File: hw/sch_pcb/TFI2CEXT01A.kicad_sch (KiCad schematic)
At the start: 17 parts, among them J2 SM04B-GHS-TB, J3 SM04B-GHS-TB, M2 M3, U3 MIC5504-3.3YM5

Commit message: Add secondary input connector #2.
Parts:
- added J?: SM04B-GHS-TB, Connector_JST:JST_GH_SM04B-GHS-TB_1x04-1MP_P1.25mm_Horizontal, symbol MLAB_CONNECTORS_JST:SM04B-GHS-TB
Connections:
- net +5V: now also J?.1
- net GND: now also J?.4, J?.MP
- net SCLin: now also J?.2
- net SDAin: now also J?.3
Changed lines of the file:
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@@
   (junction (at 81.28 168.91) (diameter 1.016) (color 0 0 0 0))
   (junction (at 91.44 102.87) (diameter 1.016) (color 0 0 0 0))
+  (junction (at 91.44 133.985) (diameter 1.016) (color 0 0 0 0))
   (junction (at 97.79 95.25) (diameter 1.016) (color 0 0 0 0))
   (junction (at 104.14 97.79) (diameter 1.016) (color 0 0 0 0))
@@
     (stroke (width 0) (type solid) (color 0 0 0 0))
   )
+  (wire (pts (xy 90.17 126.365) (xy 97.79 126.365))
+    (stroke (width 0) (type solid) (color 0 0 0 0))
+  )
+  (wire (pts (xy 90.17 128.905) (xy 97.79 128.905))
+    (stroke (width 0) (type solid) (color 0 0 0 0))
+  )
+  (wire (pts (xy 90.17 131.445) (xy 91.44 131.445))
+    (stroke (width 0) (type solid) (color 0 0 0 0))
+  )
+  (wire (pts (xy 90.17 133.985) (xy 91.44 133.985))
+    (stroke (width 0) (type solid) (color 0 0 0 0))
+  )
   (wire (pts (xy 91.44 82.55) (xy 91.44 92.71))
     (stroke (width 0) (type solid) (color 0 0 0 0))
@@
   )
   (wire (pts (xy 91.44 102.87) (xy 91.44 106.68))
+    (stroke (width 0) (type solid) (color 0 0 0 0))
+  )
+  (wire (pts (xy 91.44 119.38) (xy 91.44 123.825))
+    (stroke (width 0) (type solid) (color 0 0 0 0))
+  )
+  (wire (pts (xy 91.44 123.825) (xy 90.17 123.825))
+    (stroke (width 0) (type solid) (color 0 0 0 0))
+  )
+  (wire (pts (xy 91.44 131.445) (xy 91.44 133.985))
+    (stroke (width 0) (type solid) (color 0 0 0 0))
+  )
+  (wire (pts (xy 91.44 133.985) (xy 91.44 137.795))
     (stroke (width 0) (type solid) (color 0 0 0 0))
   )
@@
     (effects (font (size 1.524 1.524)) (justify right bottom))
   )
+  (label "SCLin" (at 97.79 126.365 180)
+    (effects (font (size 1.524 1.524)) (justify right bottom))
+  )
+  (label "SDAin" (at 97.79 128.905 180)
+    (effects (font (size 1.524 1.524)) (justify right bottom))
+  )
   (label "EN" (at 115.57 101.6 180)
     (effects (font (size 1.524 1.524)) (justify right bottom))
@@
     (pin "1")
   )
+  (symbol (lib_id "power:+5V") (at 91.44 119.38 0) (mirror y) (unit 1)
+    (in_bom yes) (on_board yes)
+    (property "Reference" "#PWR?" (id 0) (at 91.44 123.19 0)
+      (effects (font (size 1.27 1.27)) hide)
+    )
+    (property "Value" "+5V" (id 1) (at 91.059 114.9858 0))
+    (property "Footprint" "" (id 2) (at 91.44 119.38 0)
+      (effects (font (size 1.27 1.27)) hide)
+    )
+    (property "Datasheet" "" (id 3) (at 91.44 119.38 0)
+      (effects (font (size 1.27 1.27)) hide)
+    )
+    (pin "1")
+  )
   (symbol (lib_id "power:+3V3") (at 97.79 82.55 0) (unit 1)
     (in_bom yes) (on_board yes)
@@
     )
     (property "Datasheet" "" (id 3) (at 91.44 106.68 0)
+      (effects (font (size 1.27 1.27)) hide)
+    )
+    (pin "1")
+  )
+  (symbol (lib_id "power:GND") (at 91.44 137.795 0) (mirror y) (unit 1)
+    (in_bom yes) (on_board yes)
+    (property "Reference" "#PWR?" (id 0) (at 91.44 144.145 0)
+      (effects (font (size 1.27 1.27)) hide)
+    )
+    (property "Value" "GND" (id 1) (at 91.313 142.1892 0))
+    (property "Footprint" "" (id 2) (at 91.44 137.795 0)
+      (effects (font (size 1.27 1.27)) hide)
+    )
+    (property "Datasheet" "" (id 3) (at 91.44 137.795 0)
       (effects (font (size 1.27 1.27)) hide)
     )
@@
     )
     (property "UST_ID" "5c86273d1287500b4e0280be" (id 5) (at 85.09 97.79 0)
+      (effects (font (size 1.27 1.27)) hide)
+    )
+    (pin "1")
+    (pin "2")
+    (pin "3")
+    (pin "4")
+    (pin "MP")
+  )
+  (symbol (lib_id "MLAB_CONNECTORS_JST:SM04B-GHS-TB") (at 85.09 128.905 0) (mirror y) (unit 1)
+    (in_bom yes) (on_board yes)
+    (property "Reference" "J?" (id 0) (at 83.1088 127.4064 0)
+      (effects (font (size 1.524 1.524)) (justify left))
+    )
+    (property "Value" "SM04B-GHS-TB" (id 1) (at 83.1088 130.1242 0)
+      (effects (font (size 1.524 1.524)) (justify left))
+    )
+    (property "Footprint" "Connector_JST:JST_GH_SM04B-GHS-TB_1x04-1MP_P1.25mm_Horizontal" (id 2) (at 85.09 123.825 0)
+      (effects (font (size 1.524 1.524)) hide)
+    )
+    (property "Datasheet" "" (id 3) (at 85.09 123.825 0)
+      (effects (font (size 1.524 1.524)))
+    )
+    (property "UST_id" "" (id 4) (at 85.09 128.905 0)
+      (effects (font (size 1.27 1.27)) hide)
+    )
+    (property "UST_ID" "5c86273d1287500b4e0280be" (id 5) (at 85.09 128.905 0)
       (effects (font (size 1.27 1.27)) hide)
     )
@@
       (reference "#PWR?") (unit 1) (value "GND") (footprint "")
     )
+    (path "/1df0862e-b632-4bdd-aa64-2038cb83123b"
+      (reference "#PWR?") (unit 1) (value "GND") (footprint "")
+    )
     (path "/584dadcd-f462-4861-8cc5-b38ddf8e690a"
       (reference "#PWR?") (unit 1) (value "GND") (footprint "")
     )
+    (path "/6ed52263-58db-4a97-82f4-86b9f09e3aa9"
+      (reference "#PWR?") (unit 1) (value "+5V") (footprint "")
+    )
     (path "/712f2299-6d07-4921-b3fc-2767cf7d943a"
       (reference "#PWR?") (unit 1) (value "+3V3") (footprint "")
@@
       (reference "J3") (unit 1) (value "SM04B-GHS-TB") (footprint "Connector_JST:JST_GH_SM04B-GHS-TB_1x04-1MP_P1.25mm_Horizontal")
     )
+    (path "/acfde87a-c369-4ef9-b4fe-c0d5b5b283eb"
+      (reference "J?") (unit 1) (value "SM04B-GHS-TB") (footprint "Connector_JST:JST_GH_SM04B-GHS-TB_1x04-1MP_P1.25mm_Horizontal")
+    )
     (path "/cb19bc52-bc73-4faa-b1b5-9d6fa377e0e1"

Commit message: The first layout
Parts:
- added D1: LED GREEN, Mlab_D:LED_1206, symbol Device:LED
- added R1: 180R, Mlab_R:SMD-0603, symbol Device:R
- D2: renamed from D1; value ZENER-6.2V -> BZX585-B5V6.115; footprint Mlab_D:Diode-MiniMELF_Standard -> Diode_SMD:D_SOD-523
- R4: value 51R -> 180R; UST_ID 5c70984512875079b91f8953 -> (none)
- gave numbers to parts that had none: 5
- renumbered C3 to C1, C4 to C2, C1 to C3, C5 to C4, D2 to D3, J3 to J1, J2 to J3, M2 to M1, R10 to R5, R3 to R6, U3 to U1
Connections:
- net +5V: now also R1.1
- net GND: now also D1.1 (K)
- new net: D1.2 (A), R1.2
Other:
- note removed: "BZX585-B5V6.115 NEXPERIA"

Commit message: Edit PCB
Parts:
- added M2, M3, M4, M5, M6: HOLE, Mlab_Mechanical:dira_3mm, symbol MLAB_MECHANICAL:HOLE
- M1: value M3 -> HOLE; footprint Mlab_Mechanical:MountingHole_3mm -> Mlab_Mechanical:dira_3mm
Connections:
- net GND: no longer M1.1
- no-connect marks 0 -> 6
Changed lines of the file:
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@@
-(kicad_sch (version 20210126) (generator eeschema)
+(kicad_sch (version 20210406) (generator eeschema)
   (paper "A4")
   (title_block
@@
   (junction (at 161.29 102.87) (diameter 1.016) (color 0 0 0 0))
   (junction (at 161.29 129.54) (diameter 1.016) (color 0 0 0 0))
+  (no_connect (at 228.6 20.32))
+  (no_connect (at 237.49 20.32))
+  (no_connect (at 246.38 20.32))
+  (no_connect (at 255.27 20.32))
+  (no_connect (at 264.16 20.32))
+  (no_connect (at 273.05 20.32))
   (wire (pts (xy 19.05 163.83) (xy 19.05 165.1))
     (stroke (width 0) (type solid) (color 0 0 0 0))
@@
     (stroke (width 0) (type solid) (color 0 0 0 0))
   )
-  (wire (pts (xy 265.43 20.32) (xy 265.43 19.05))
-    (stroke (width 0) (type solid) (color 0 0 0 0))
-  )
-  (wire (pts (xy 270.51 19.05) (xy 265.43 19.05))
-    (stroke (width 0) (type solid) (color 0 0 0 0))
-  )
-  (wire (pts (xy 270.51 20.32) (xy 270.51 19.05))
-    (stroke (width 0) (type solid) (color 0 0 0 0))
-  )
-  (polyline (pts (xy 255.27 17.78) (xy 280.67 17.78))
+  (polyline (pts (xy 226.06 17.78) (xy 229.87 17.78))
     (stroke (width 0) (type dash) (color 0 0 0 0))
   )
-  (polyline (pts (xy 255.27 27.94) (xy 255.27 17.78))
+  (polyline (pts (xy 226.06 27.94) (xy 226.06 17.78))
+    (stroke (width 0) (type dash) (color 0 0 0 0))
+  )
+  (polyline (pts (xy 226.06 27.94) (xy 229.87 27.94))
+    (stroke (width 0) (type dash) (color 0 0 0 0))
+  )
+  (polyline (pts (xy 229.87 17.78) (xy 237.49 17.78))
+    (stroke (width 0) (type dash) (color 0 0 0 0))
+  )
+  (polyline (pts (xy 229.87 27.94) (xy 237.49 27.94))
+    (stroke (width 0) (type dash) (color 0 0 0 0))
+  )
+  (polyline (pts (xy 237.49 17.78) (xy 262.89 17.78))
+    (stroke (width 0) (type dash) (color 0 0 0 0))
+  )
+  (polyline (pts (xy 262.89 17.78) (xy 280.67 17.78))
+    (stroke (width 0) (type dash) (color 0 0 0 0))
+  )
+  (polyline (pts (xy 262.89 27.94) (xy 237.49 27.94))
+    (stroke (width 0) (type dash) (color 0 0 0 0))
+  )
+  (polyline (pts (xy 262.89 27.94) (xy 280.67 27.94))
     (stroke (width 0) (type dash) (color 0 0 0 0))
   )
@@
     (stroke (width 0) (type dash) (color 0 0 0 0))
   )
-  (polyline (pts (xy 280.67 27.94) (xy 255.27 27.94))
-    (stroke (width 0) (type dash) (color 0 0 0 0))
-  )
-  (text "MOUNTING HOLES" (at 257.81 27.94 0)
+  (text "MOUNTING HOLES" (at 240.03 27.94 0)
     (effects (font (size 1.524 1.524)) (justify left bottom))
   )
@@
     (effects (font (size 1.524 1.524)) (justify left bottom))
   )
-  (symbol (lib_id "MLAB_MECHANICAL:HOLE") (at 265.43 21.59 90) (unit 1)
-    (in_bom yes) (on_board yes)
-    (property "Reference" "M1" (id 0) (at 265.43 24.13 90)
-      (effects (font (size 1.524 1.524)))
-    )
-    (property "Value" "M3" (id 1) (at 262.89 20.32 0)
-      (effects (font (size 1.524 1.524)))
-    )
-    (property "Footprint" "Mlab_Mechanical:MountingHole_3mm" (id 2) (at 265.43 21.59 0)
-      (effects (font (size 1.524 1.524)) hide)
-    )
-    (property "Datasheet" "" (id 3) (at 265.43 21.59 0)
+  (symbol (lib_id "MLAB_MECHANICAL:HOLE") (at 228.6 21.59 90) (unit 1)
+    (in_bom yes) (on_board yes) (fields_autoplaced)
+    (property "Reference" "M1" (id 0) (at 229.9971 20.2579 90)
+      (effects (font (size 1.524 1.524)) (justify right))
+    )
+    (property "Value" "HOLE" (id 1) (at 229.9971 22.9655 90)
+      (effects (font (size 1.524 1.524)) (justify right))
+    )
+    (property "Footprint" "Mlab_Mechanical:dira_3mm" (id 2) (at 228.6 21.59 0)
+      (effects (font (size 1.524 1.524)) hide)
+    )
+    (property "Datasheet" "" (id 3) (at 228.6 21.59 0)
+      (effects (font (size 1.524 1.524)))
+    )
+    (pin "1")
+  )
+  (symbol (lib_id "MLAB_MECHANICAL:HOLE") (at 237.49 21.59 90) (unit 1)
+    (in_bom yes) (on_board yes) (fields_autoplaced)
+    (property "Reference" "M2" (id 0) (at 238.8871 20.2579 90)
+      (effects (font (size 1.524 1.524)) (justify right))
+    )
+    (property "Value" "HOLE" (id 1) (at 238.8871 22.9655 90)
+      (effects (font (size 1.524 1.524)) (justify right))
+    )
+    (property "Footprint" "Mlab_Mechanical:dira_3mm" (id 2) (at 237.49 21.59 0)
+      (effects (font (size 1.524 1.524)) hide)
+    )
+    (property "Datasheet" "" (id 3) (at 237.49 21.59 0)
+      (effects (font (size 1.524 1.524)))
+    )
+    (pin "1")
+  )
+  (symbol (lib_id "MLAB_MECHANICAL:HOLE") (at 246.38 21.59 90) (unit 1)
+    (in_bom yes) (on_board yes)
+    (property "Reference" "M3" (id 0) (at 247.7771 20.2579 90)
+      (effects (font (size 1.524 1.524)) (justify right))
+    )
+    (property "Value" "HOLE" (id 1) (at 247.7771 22.9655 90)
+      (effects (font (size 1.524 1.524)) (justify right))
+    )
+    (property "Footprint" "Mlab_Mechanical:dira_3mm" (id 2) (at 246.38 21.59 0)
+      (effects (font (size 1.524 1.524)) hide)
+    )
+    (property "Datasheet" "" (id 3) (at 246.38 21.59 0)
+      (effects (font (size 1.524 1.524)))
+    )
+    (pin "1")
+  )
+  (symbol (lib_id "MLAB_MECHANICAL:HOLE") (at 255.27 21.59 90) (unit 1)
+    (in_bom yes) (on_board yes) (fields_autoplaced)
+    (property "Reference" "M4" (id 0) (at 256.6671 20.2579 90)
+      (effects (font (size 1.524 1.524)) (justify right))
+    )
+    (property "Value" "HOLE" (id 1) (at 256.6671 22.9655 90)
+      (effects (font (size 1.524 1.524)) (justify right))
+    )
+    (property "Footprint" "Mlab_Mechanical:dira_3mm" (id 2) (at 255.27 21.59 0)
+      (effects (font (size 1.524 1.524)) hide)
+    )
+    (property "Datasheet" "" (id 3) (at 255.27 21.59 0)
+      (effects (font (size 1.524 1.524)))
+    )
+    (pin "1")
+  )
+  (symbol (lib_id "MLAB_MECHANICAL:HOLE") (at 264.16 21.59 90) (unit 1)
+    (in_bom yes) (on_board yes) (fields_autoplaced)
+    (property "Reference" "M5" (id 0) (at 265.5571 20.2579 90)
+      (effects (font (size 1.524 1.524)) (justify right))
+    )
+    (property "Value" "HOLE" (id 1) (at 265.5571 22.9655 90)
+      (effects (font (size 1.524 1.524)) (justify right))
+    )
+    (property "Footprint" "Mlab_Mechanical:dira_3mm" (id 2) (at 264.16 21.59 0)
+      (effects (font (size 1.524 1.524)) hide)
+    )
+    (property "Datasheet" "" (id 3) (at 264.16 21.59 0)
+      (effects (font (size 1.524 1.524)))
+    )
+    (pin "1")
+  )
+  (symbol (lib_id "MLAB_MECHANICAL:HOLE") (at 273.05 21.59 90) (unit 1)
+    (in_bom yes) (on_board yes) (fields_autoplaced)
+    (property "Reference" "M6" (id 0) (at 274.4471 20.2579 90)
+      (effects (font (size 1.524 1.524)) (justify right))
+    )
+    (property "Value" "HOLE" (id 1) (at 274.4471 22.9655 90)
+      (effects (font (size 1.524 1.524)) (justify right))
+    )
+    (property "Footprint" "Mlab_Mechanical:dira_3mm" (id 2) (at 273.05 21.59 0)
+      (effects (font (size 1.524 1.524)) hide)
+    )
+    (property "Datasheet" "" (id 3) (at 273.05 21.59 0)
       (effects (font (size 1.524 1.524)))
     )
@@
     (property "Datasheet" "" (id 3) (at 161.29 132.08 0)
       (effects (font (size 1.27 1.27)) hide)
-    )
-    (pin "1")
-  )
-  (symbol (lib_id "power:GND") (at 270.51 20.32 0) (unit 1)
-    (in_bom yes) (on_board yes)
-    (property "Reference" "#PWR027" (id 0) (at 270.51 26.67 0)
-      (effects (font (size 1.524 1.524)) hide)
-    )
-    (property "Value" "GND" (id 1) (at 270.51 24.13 0)
-      (effects (font (size 1.524 1.524)))
-    )
-    (property "Footprint" "" (id 2) (at 270.51 20.32 0)
-      (effects (font (size 1.524 1.524)))
-    )
-    (property "Datasheet" "" (id 3) (at 270.51 20.32 0)
-      (effects (font (size 1.524 1.524)))
     )
     (pin "1")
@@
       (reference "#PWR026") (unit 1) (value "GND") (footprint "")
     )
-    (path "/00000000-0000-0000-0000-0000549d770f"
-      (reference "#PWR027") (unit 1) (value "GND") (footprint "")
-    )
     (path "/00000000-0000-0000-0000-000059ffc6a8"
       (reference "C1") (unit 1) (value "10uF") (footprint "Mlab_R:SMD-0805")
@@
       (reference "J4") (unit 1) (value "SM04B-GHS-TB") (footprint "Connector_JST:JST_GH_SM04B-GHS-TB_1x04-1MP_P1.25mm_Horizontal")
     )
-    (path "/00000000-0000-0000-0000-0000549d7628"
-      (reference "M1") (unit 1) (value "M3") (footprint "Mlab_Mechanical:MountingHole_3mm")
+    (path "/99d533fb-9d70-48e2-8fd6-c2f3a8e6e539"
+      (reference "M1") (unit 1) (value "HOLE") (footprint "Mlab_Mechanical:dira_3mm")
+    )
+    (path "/5772f8cf-ad63-4406-98f0-cba007b77f95"
+      (reference "M2") (unit 1) (value "HOLE") (footprint "Mlab_Mechanical:dira_3mm")
+    )
+    (path "/274711c1-bbe2-42ee-96d7-8e3e40bc8d5d"
+      (reference "M3") (unit 1) (value "HOLE") (footprint "Mlab_Mechanical:dira_3mm")
+    )
+    (path "/21d93760-b684-44de-bfcd-0dfe3feb2abe"
+      (reference "M4") (unit 1) (value "HOLE") (footprint "Mlab_Mechanical:dira_3mm")
+    )
+    (path "/dcef6574-268c-4858-9322-b68348606397"
+      (reference "M5") (unit 1) (value "HOLE") (footprint "Mlab_Mechanical:dira_3mm")
+    )
+    (path "/19b0d29d-d7c2-446e-a8fb-72bf37c91050"
+      (reference "M6") (unit 1) (value "HOLE") (footprint "Mlab_Mechanical:dira_3mm")
     )
     (path "/d6f125ac-9f23-4a8a-8f1d-fc20a4cd2a4a"

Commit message: Edit
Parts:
- D1: UST_ID (none) -> 5c70984412875079b91f8895
- D2: UST_ID 604b0326128750769e5b0f93 -> 60879d38128750769ee58e48
- R1, R4: UST_ID (none) -> 5c70984512875079b91f8957
- R2, R3, R5, R6: UST_ID 5c70984612875079b91f899f -> 5c70984512875079b91f8962
- U2: UST_ID (none) -> 6087a3f3128750769ee58f03
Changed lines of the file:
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@@
       (effects (font (size 1.27 1.27)) hide)
     )
-    (property "UST_ID" "" (id 5) (at 19.05 168.91 0)
+    (property "UST_ID" "5c70984512875079b91f8957" (id 5) (at 19.05 168.91 0)
       (effects (font (size 1.27 1.27)) hide)
     )
@@
       (effects (font (size 1.27 1.27)) hide)
     )
-    (property "UST_ID" "5c70984612875079b91f899f" (id 5) (at 97.79 87.63 0)
+    (property "UST_ID" "5c70984512875079b91f8962" (id 5) (at 97.79 87.63 0)
       (effects (font (size 1.27 1.27)) hide)
     )
@@
       (effects (font (size 1.27 1.27)) hide)
     )
-    (property "UST_ID" "5c70984612875079b91f899f" (id 5) (at 104.14 87.63 0)
+    (property "UST_ID" "5c70984512875079b91f8962" (id 5) (at 104.14 87.63 0)
       (effects (font (size 1.27 1.27)) hide)
     )
@@
       (effects (font (size 1.27 1.27)) hide)
     )
-    (property "UST_ID" "" (id 5) (at 140.97 87.63 0)
+    (property "UST_ID" "5c70984512875079b91f8957" (id 5) (at 140.97 87.63 0)
       (effects (font (size 1.27 1.27)) hide)
     )
@@
       (effects (font (size 1.27 1.27)) hide)
     )
-    (property "UST_ID" "5c70984612875079b91f899f" (id 5) (at 147.32 87.63 0)
+    (property "UST_ID" "5c70984512875079b91f8962" (id 5) (at 147.32 87.63 0)
       (effects (font (size 1.27 1.27)) hide)
     )
@@
       (effects (font (size 1.27 1.27)) hide)
     )
-    (property "UST_ID" "5c70984612875079b91f899f" (id 5) (at 153.67 87.63 0)
+    (property "UST_ID" "5c70984512875079b91f8962" (id 5) (at 153.67 87.63 0)
       (effects (font (size 1.27 1.27)) hide)
     )
@@
       (effects (font (size 1.27 1.27)) hide)
     )
-    (property "UST_ID" "604b0326128750769e5b0f93" (id 5) (at 43.18 175.26 0)
+    (property "UST_ID" "60879d38128750769ee58e48" (id 5) (at 43.18 175.26 0)
       (effects (font (size 1.27 1.27)) hide)
     )
@@
       (effects (font (size 1.27 1.27)) hide)
     )
-    (property "UST_ID" "" (id 5) (at 19.05 177.8 0)
+    (property "UST_ID" "5c70984412875079b91f8895" (id 5) (at 19.05 177.8 0)
       (effects (font (size 1.27 1.27)) hide)
     )
@@
       (effects (font (size 1.27 1.27)) hide)
     )
+    (property "UST_ID" "6087a3f3128750769ee58f03" (id 4) (at 125.73 97.79 0)
+      (effects (font (size 1.27 1.27)) hide)
+    )

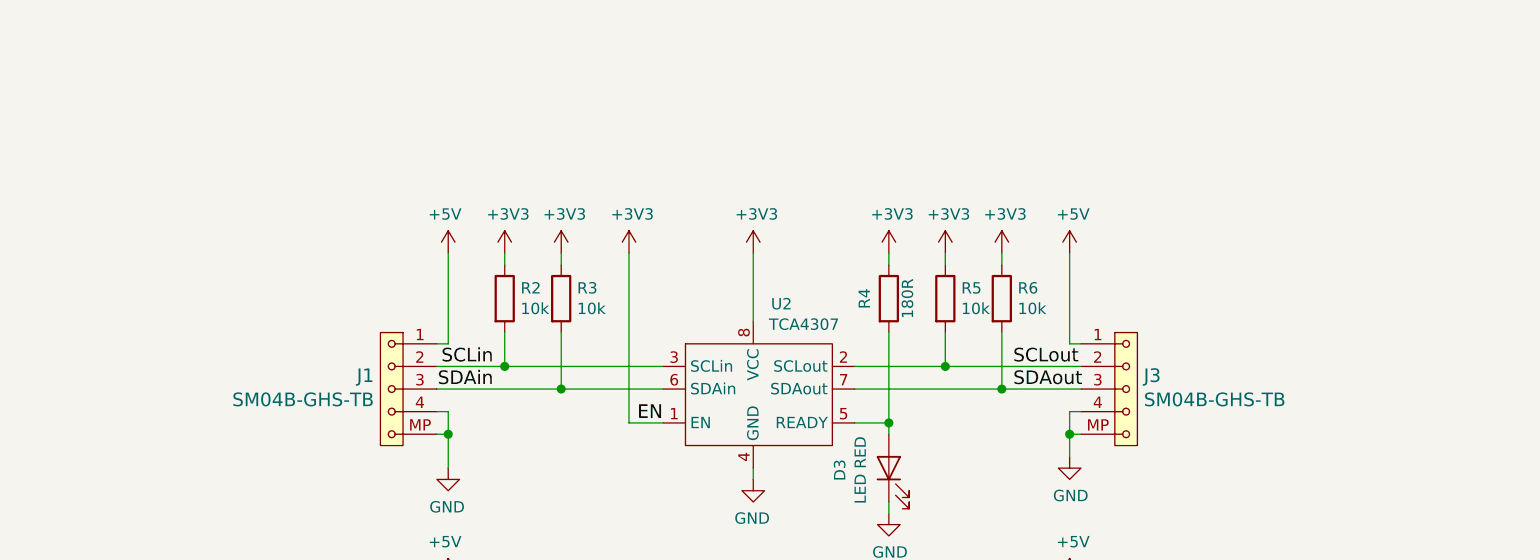
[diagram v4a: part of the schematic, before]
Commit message: Improved Slave and Master side marking. #6.
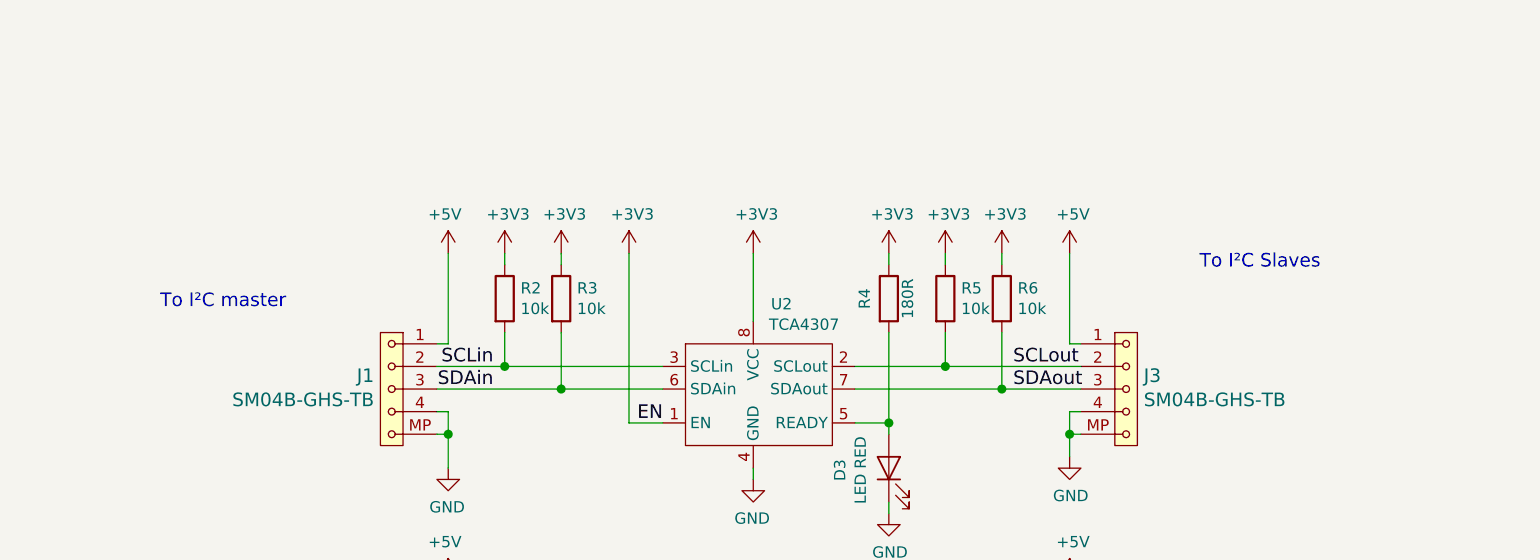
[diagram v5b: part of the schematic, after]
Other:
- note added: "To I²C Slaves"
- note added: "To I²C master"
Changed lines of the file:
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@@
     (stroke (width 0) (type dash) (color 0 0 0 0))
+  )
+  (text "To I²C master" (at 59.055 88.9 0)
+    (effects (font (size 1.524 1.524)) (justify left bottom))
+  )
+  (text "To I²C Slaves" (at 175.895 84.455 0)
+    (effects (font (size 1.524 1.524)) (justify left bottom))
   )
   (text "MOUNTING HOLES" (at 240.03 27.94 0)
